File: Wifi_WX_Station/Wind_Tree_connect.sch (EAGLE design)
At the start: 4 parts, among them J1 RJ45-8VERT

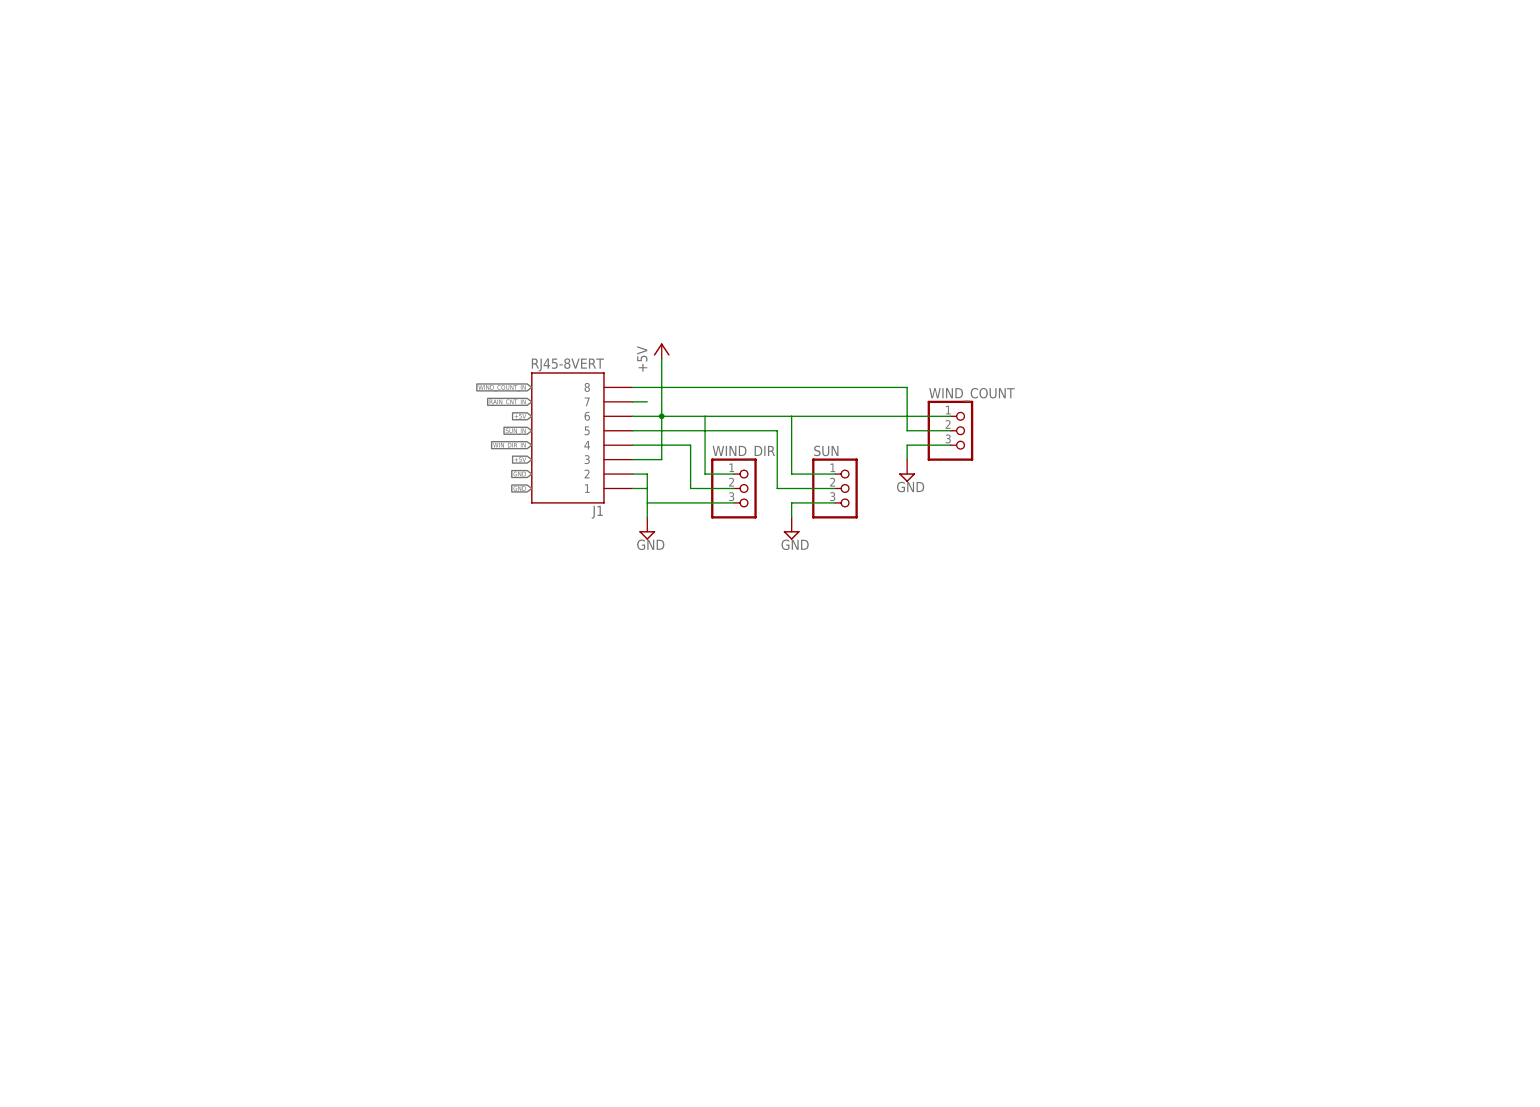
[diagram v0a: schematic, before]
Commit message: added SILabs Hygrometer board Added frames to the schematics
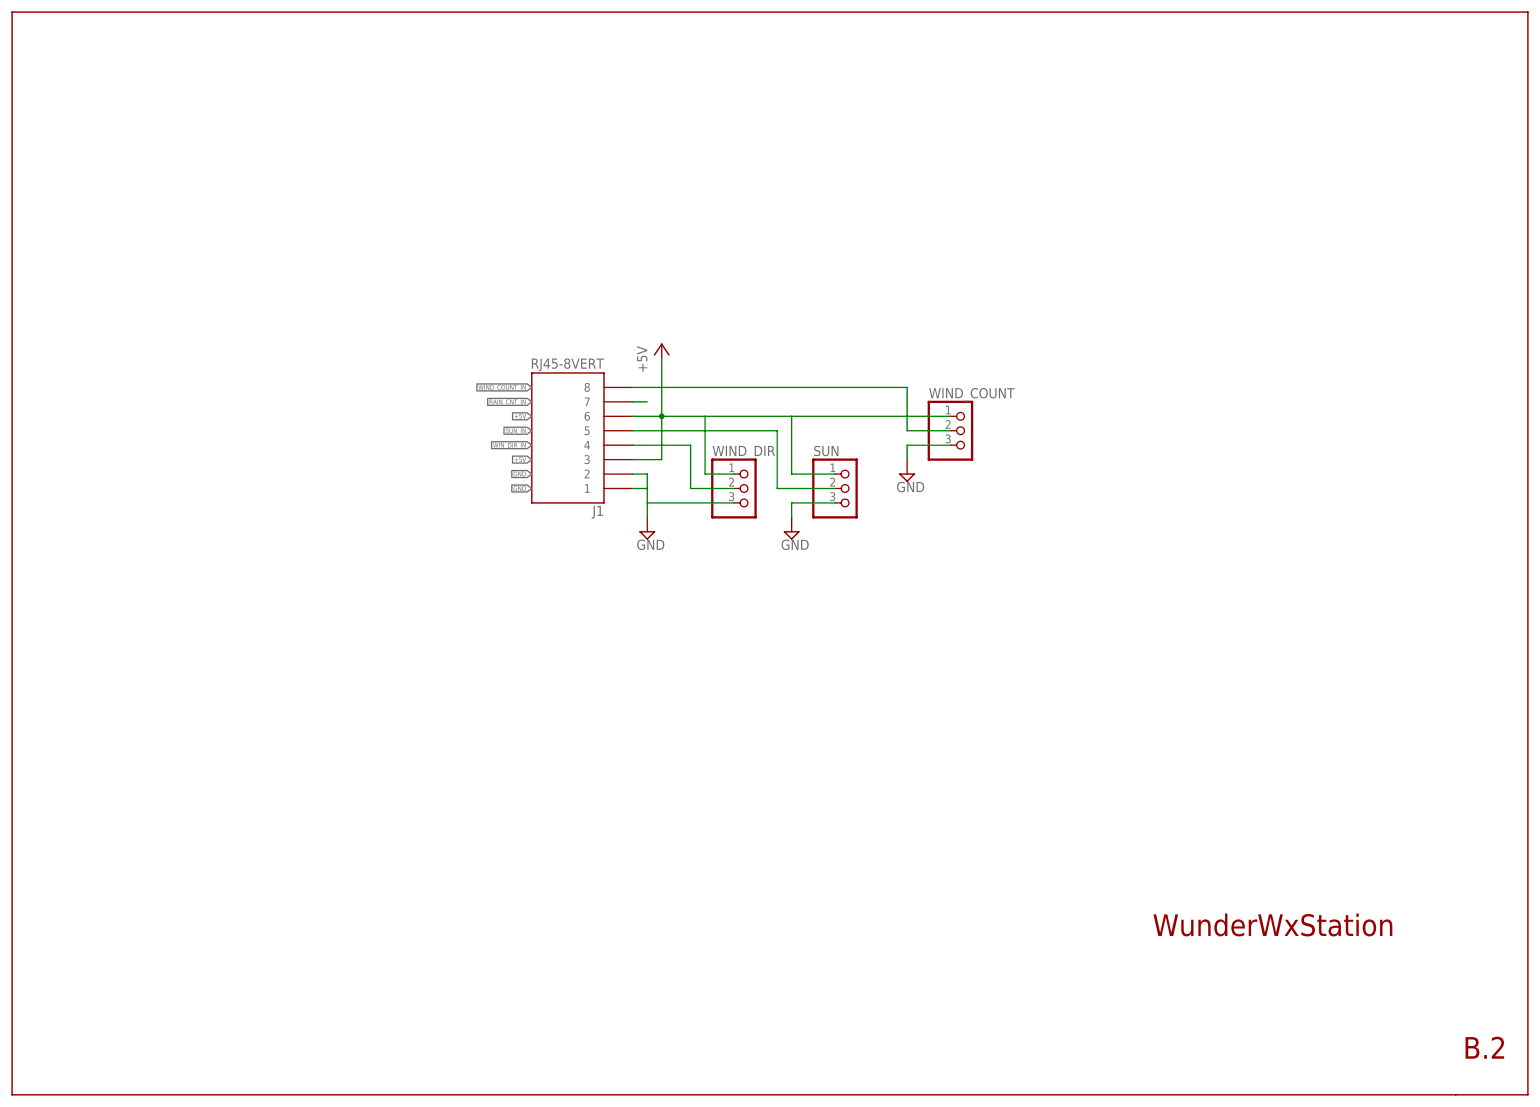
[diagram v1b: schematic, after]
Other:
- note added: "B.2"
- note added: "WunderWxStation"
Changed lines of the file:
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@@
 <part name="SUN" library="wifi_WX" deviceset="PINHD-1X3" device=""/>
 <part name="SUPPLY2" library="supply2" deviceset="GND" device=""/>
+<part name="U$1" library="1AA_Stofer" deviceset="8.5X11" device=""/>
 </parts>
 <sheets>
 <sheet>
 <plain>
+<text x="195.58" y="-33.02" size="3.81" layer="94" ratio="20">WunderWxStation</text>
+<text x="250.19" y="-54.61" size="3.81" layer="94" ratio="20">B.2</text>
 </plain>
 <instances>
@@
 <instance part="SUN" gate="A" x="142.24" y="45.72"/>
 <instance part="SUPPLY2" gate="GND" x="132.08" y="38.1"/>
+<instance part="U$1" gate="G$1" x="-5.08" y="-60.96"/>
+<instance part="U$1" gate="G$2" x="160.02" y="-60.96"/>
 </instances>
 <busses>

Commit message: Added multiple new boards - H-pwrdist- Insp_Wind_enc, 5040 etc..
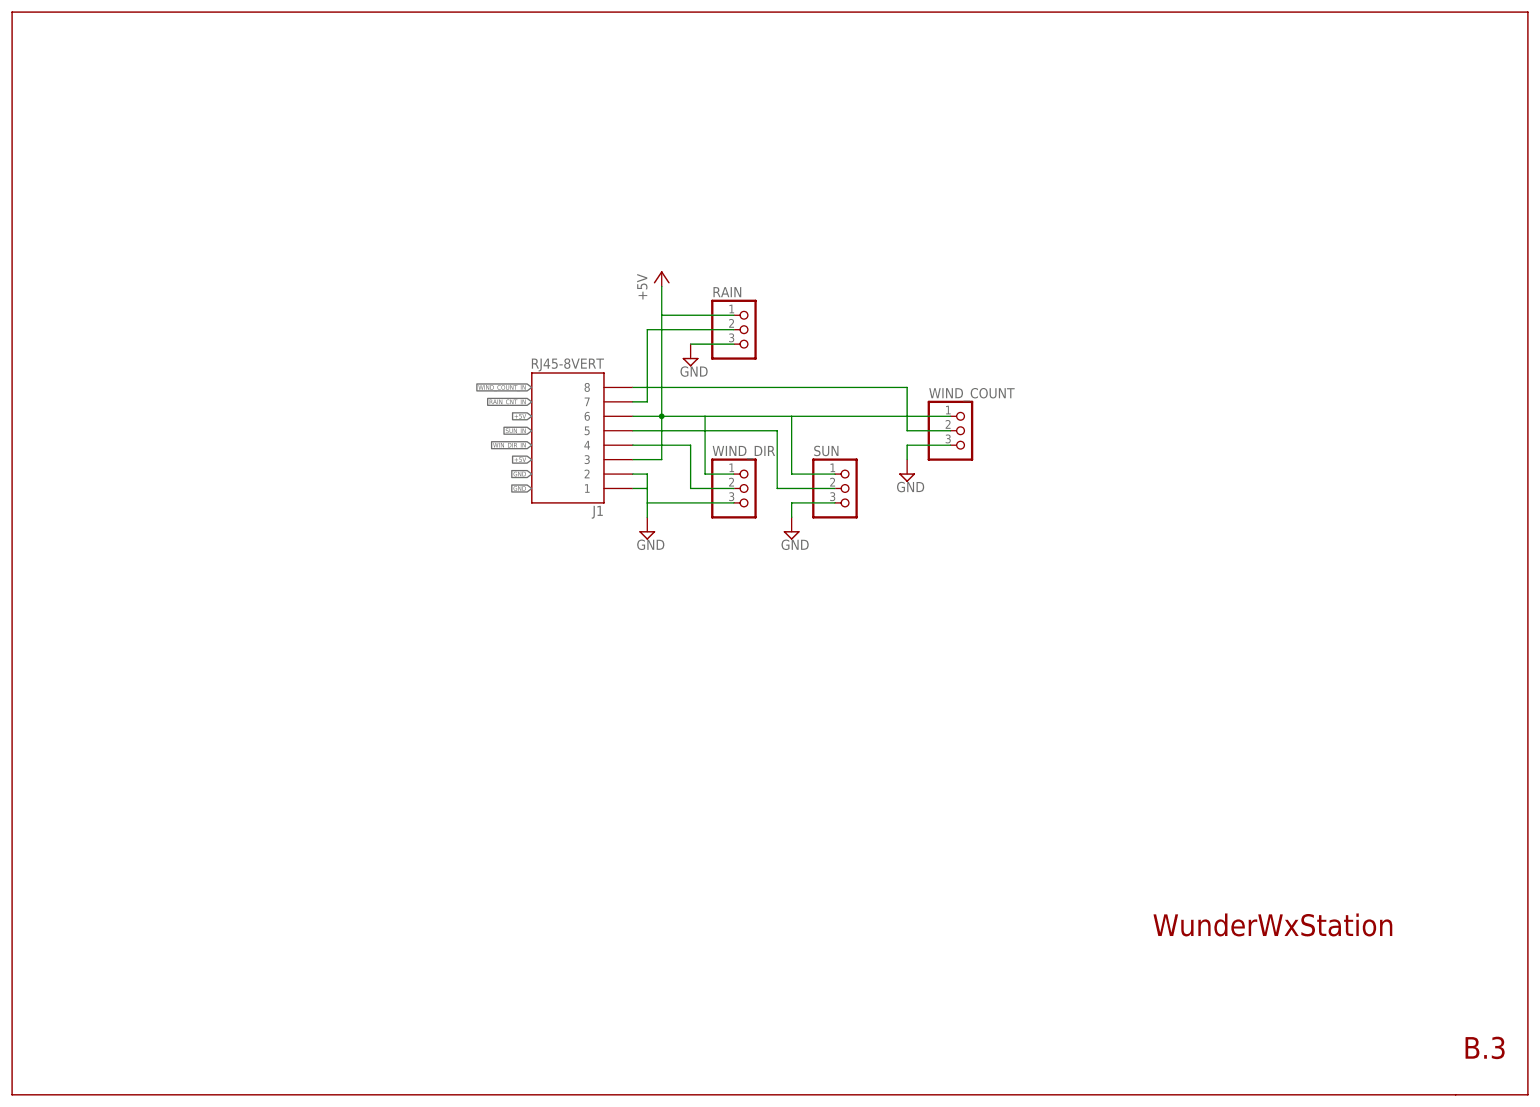
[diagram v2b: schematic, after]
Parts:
- added RAIN: (no value), wifi_WX:PINHD-1X3
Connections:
- net +5V: now also RAIN.1
- net GND: now also RAIN.3
- net RAIN_CNT_IN: now also RAIN.2
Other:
- note added: "B.3"
- note removed: "B.2"
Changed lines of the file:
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@@
 <part name="SUPPLY2" library="supply2" deviceset="GND" device=""/>
 <part name="U$1" library="1AA_Stofer" deviceset="8.5X11" device=""/>
+<part name="RAIN" library="wifi_WX" deviceset="PINHD-1X3" device=""/>
+<part name="SUPPLY3" library="supply2" deviceset="GND" device=""/>
 </parts>
 <sheets>
@@
 <plain>
 <text x="195.58" y="-33.02" size="3.81" layer="94" ratio="20">WunderWxStation</text>
-<text x="250.19" y="-54.61" size="3.81" layer="94" ratio="20">B.2</text>
+<text x="250.19" y="-54.61" size="3.81" layer="94" ratio="20">B.3</text>
 </plain>
 <instances>
 <instance part="SUPPLY20" gate="GND" x="106.68" y="38.1"/>
 <instance part="J1" gate="G$1" x="91.44" y="55.88" rot="R180"/>
-<instance part="P+3" gate="1" x="109.22" y="71.12"/>
+<instance part="P+3" gate="1" x="109.22" y="83.82"/>
 <instance part="WIND_DIR" gate="A" x="124.46" y="45.72"/>
 <instance part="WIND_COUNT" gate="A" x="162.56" y="55.88"/>
@@
 <instance part="U$1" gate="G$1" x="-5.08" y="-60.96"/>
 <instance part="U$1" gate="G$2" x="160.02" y="-60.96"/>
+<instance part="RAIN" gate="A" x="124.46" y="73.66"/>
+<instance part="SUPPLY3" gate="GND" x="114.3" y="68.58"/>
 </instances>
 <busses>
@@
 <pinref part="SUPPLY2" gate="GND" pin="GND"/>
 </segment>
+<segment>
+<pinref part="RAIN" gate="A" pin="3"/>
+<wire x1="121.92" y1="71.12" x2="114.3" y2="71.12" width="0.1524" layer="91"/>
+<pinref part="SUPPLY3" gate="GND" pin="GND"/>
+</segment>
 </net>
 <net name="+5V" class="0">
@@
 <wire x1="116.84" y1="48.26" x2="121.92" y2="48.26" width="0.1524" layer="91"/>
 <pinref part="P+3" gate="1" pin="+5V"/>
-<wire x1="109.22" y1="68.58" x2="109.22" y2="58.42" width="0.1524" layer="91"/>
+<wire x1="109.22" y1="76.2" x2="109.22" y2="58.42" width="0.1524" layer="91"/>
 <wire x1="116.84" y1="58.42" x2="132.08" y2="58.42" width="0.1524" layer="91"/>
 <pinref part="WIND_COUNT" gate="A" pin="1"/>
@@
 <pinref part="SUN" gate="A" pin="1"/>
 <wire x1="132.08" y1="48.26" x2="139.7" y2="48.26" width="0.1524" layer="91"/>
+<pinref part="RAIN" gate="A" pin="1"/>
+<wire x1="121.92" y1="76.2" x2="109.22" y2="76.2" width="0.1524" layer="91"/>
+<wire x1="109.22" y1="76.2" x2="109.22" y2="81.28" width="0.1524" layer="91"/>
 </segment>
 </net>
@@
 <wire x1="106.68" y1="60.96" x2="104.14" y2="60.96" width="0.1524" layer="91"/>
 <pinref part="J1" gate="G$1" pin="7"/>
+<wire x1="106.68" y1="60.96" x2="106.68" y2="73.66" width="0.1524" layer="91"/>
+<pinref part="RAIN" gate="A" pin="2"/>
+<wire x1="106.68" y1="73.66" x2="121.92" y2="73.66" width="0.1524" layer="91"/>
 </segment>
 </net>
